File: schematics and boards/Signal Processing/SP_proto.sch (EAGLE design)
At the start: 30 parts, among them IC1 MAX490CPA+, IC2 MAX490CPA+, IC3 MAX490CPA+, IC4 MAX490CPA+, IC6 MEGA164-P, IC7 MAX490CPA+, Q1 20MHz

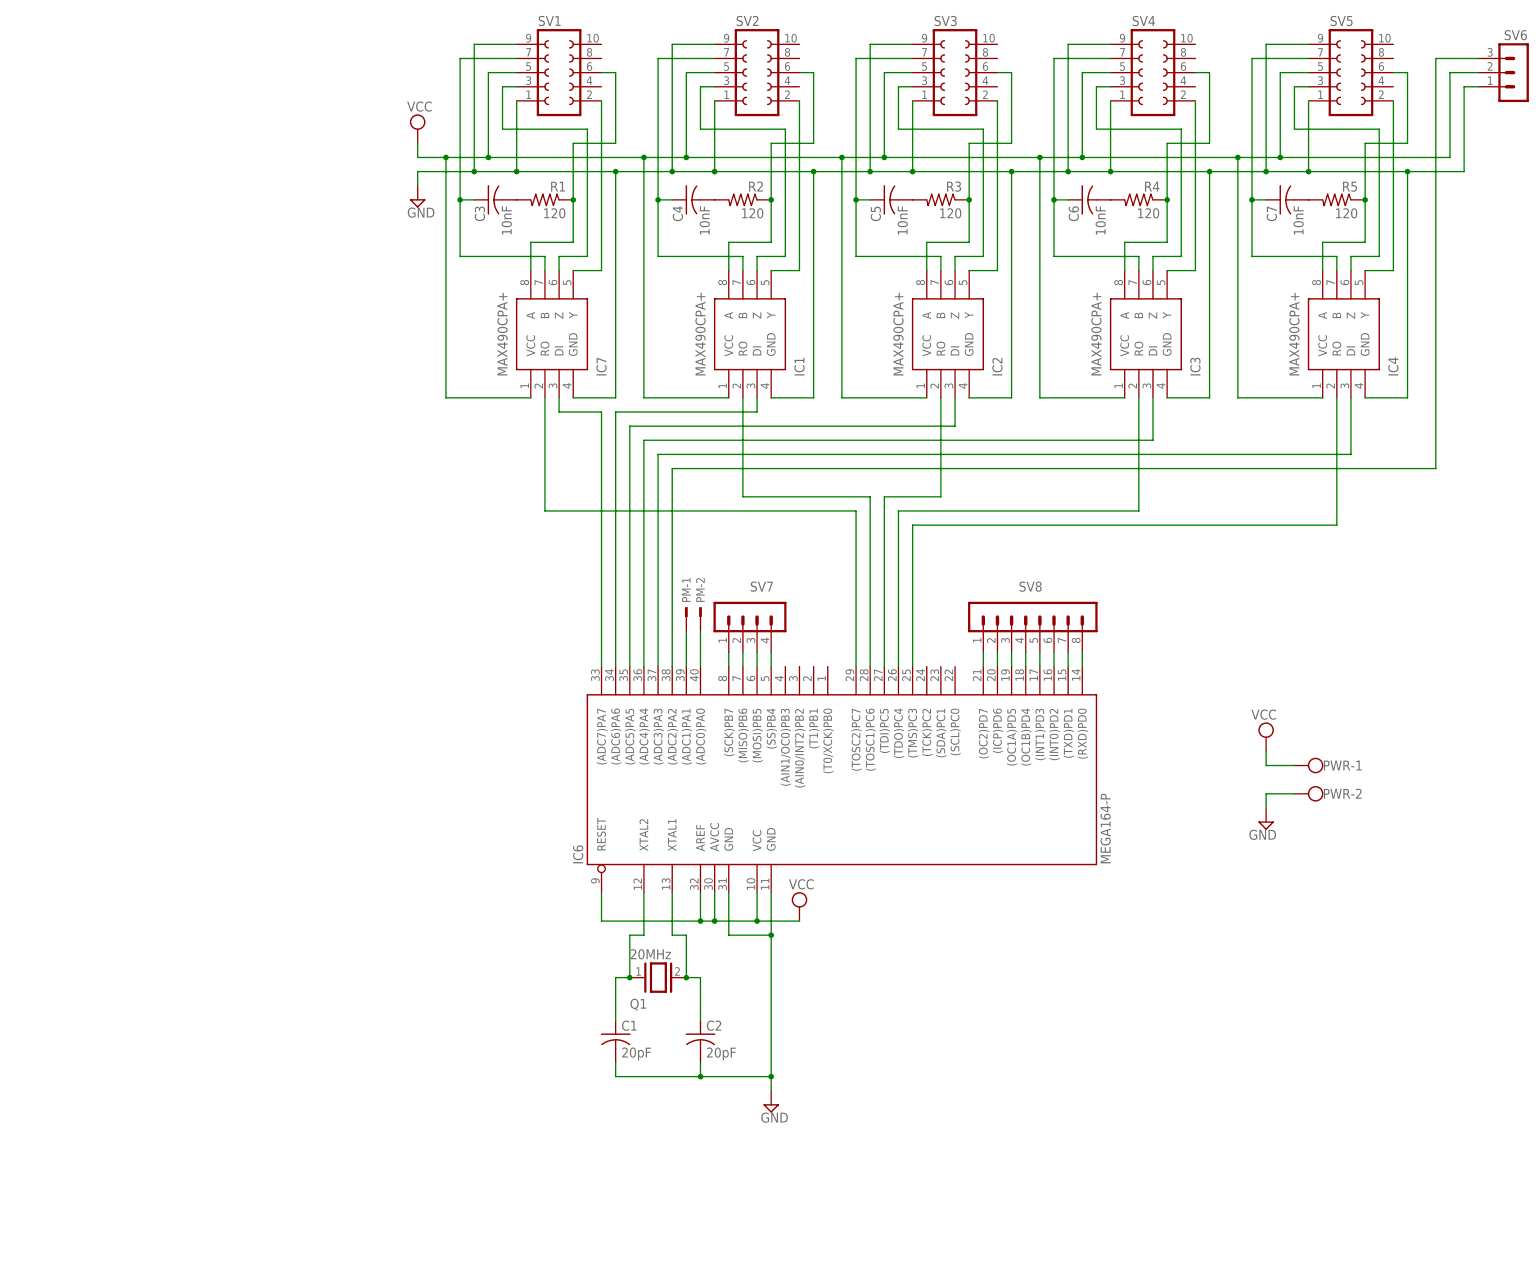
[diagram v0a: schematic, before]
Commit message: Made a small change in the Power Distribution board within the new 5th version. Cleaned up the schematic names and got rid of outdated or useless schematic and board files.
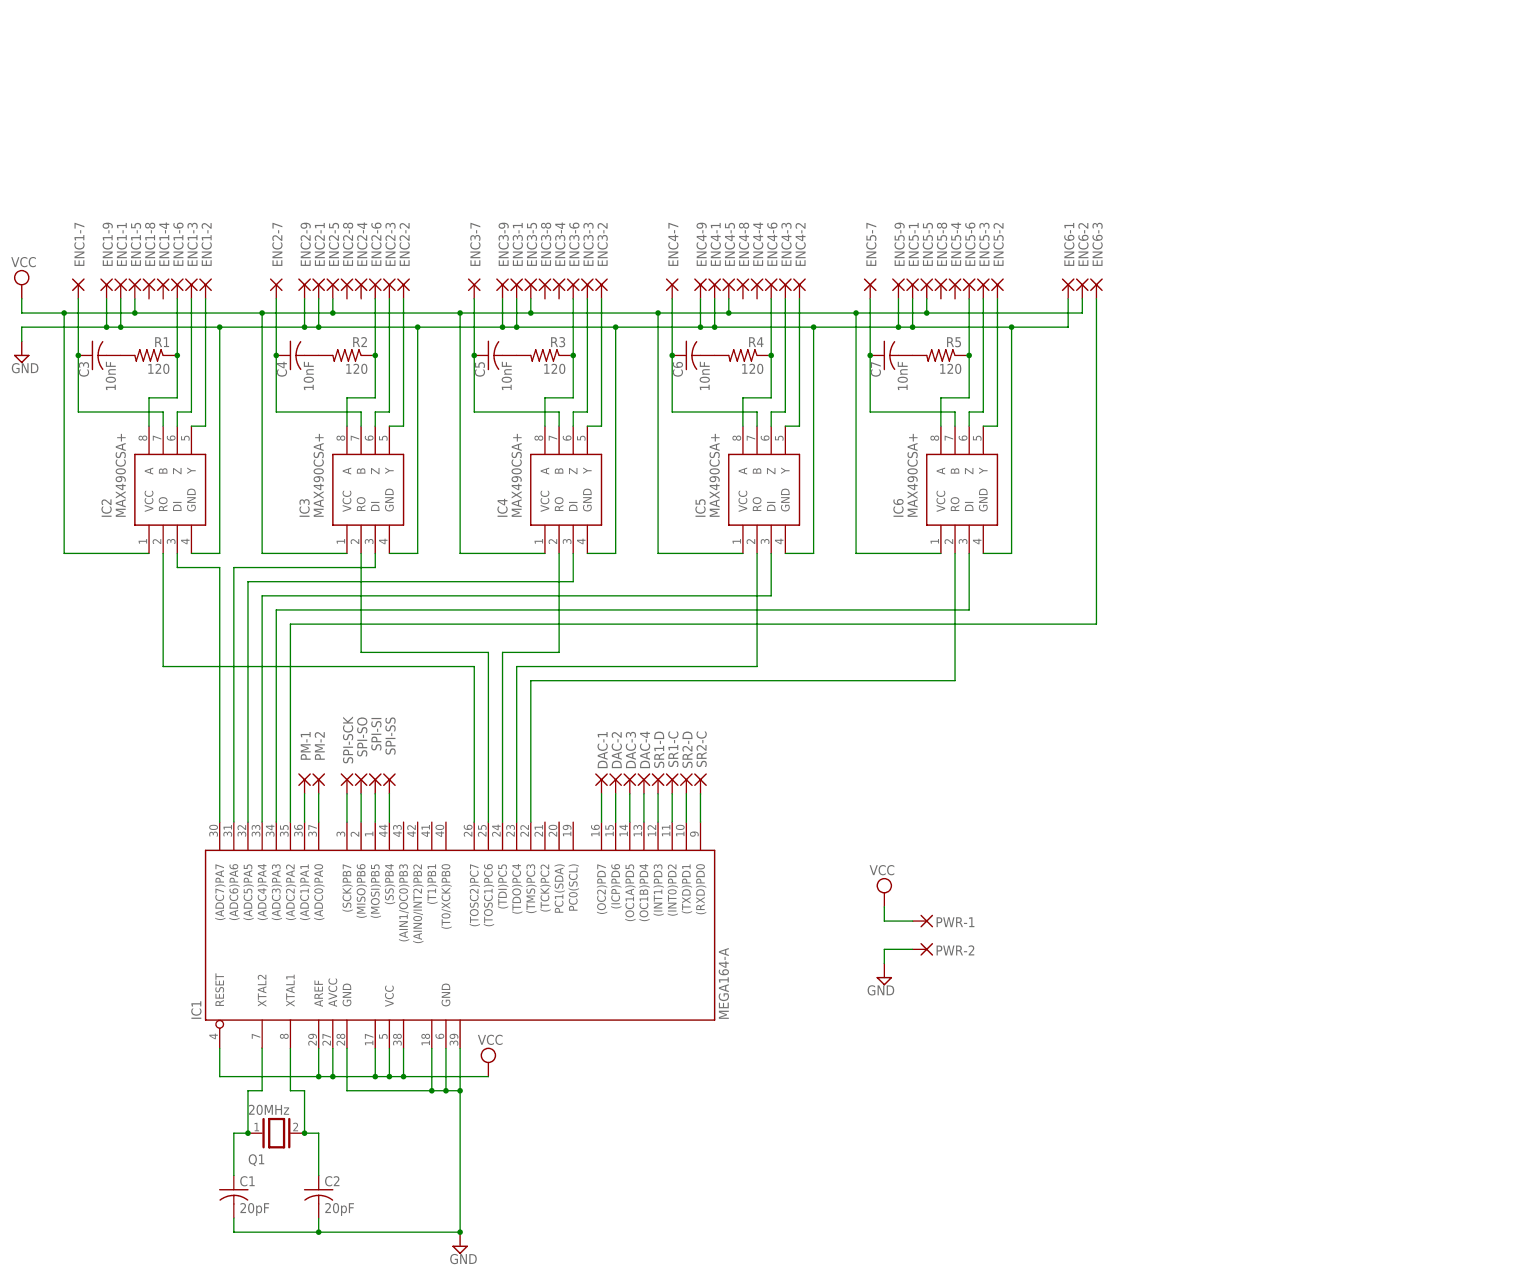
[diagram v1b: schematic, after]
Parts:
- removed IC7: MAX490CPA+, rasm_parts:MAX490CPA+
- removed PWR: (no value), con-wago-500:W237-102
- removed SV1, SV2, SV3, SV4, SV5: (no value), con-lsta:FE05-2
- removed SV6: (no value), con-lstb:MA03-1
- removed SV7: (no value), con-lstb:MA04-1
- removed SV8: (no value), con-lstb:MA08-1W
- added DAC-1, DAC-2, DAC-3, DAC-4, ENC1-1, ENC1-2, ENC1-3, ENC1-4, ENC1-5, ENC1-6, ENC1-7, ENC1-8, ENC1-9, ENC2-1, ENC2-2, ENC2-3, ENC2-4, ENC2-5, ENC2-6, ENC2-7, ENC2-8, ENC2-9, ENC3-1, ENC3-2, ENC3-3, ENC3-4, ENC3-5, ENC3-6, ENC3-7, ENC3-8, ENC3-9, ENC4-1, ENC4-2, ENC4-3, ENC4-4, ENC4-5, ENC4-6, ENC4-7, ENC4-8, ENC4-9, ENC5-1, ENC5-2, ENC5-3, ENC5-4, ENC5-5, ENC5-6, ENC5-7, ENC5-8, ENC5-9, ENC6-1, ENC6-2, ENC6-3, PWR-1, PWR-2, SPI-SCK, SPI-SI, SPI-SO, SPI-SS, SR1-C, SR1-D, SR2-C, SR2-D: (no value), wirepad:1,6/0,8
- added IC5: MAX490CSA+, rasm_parts:MAX490CSA+
- IC1: value MAX490CPA+ -> MEGA164-A; device rasm_parts:MAX490CPA+ -> atmel:MEGA16-A
- IC2, IC3, IC4: value MAX490CPA+ -> MAX490CSA+; device rasm_parts:MAX490CPA+ -> rasm_parts:MAX490CSA+
- IC6: value MEGA164-P -> MAX490CSA+; device atmel:MEGA16-P -> rasm_parts:MAX490CSA+
- PM-1, PM-2: value TSW-101-07-G-S -> (none); device con-samtec:TSW-101-07-G-S -> wirepad:1,6/0,8
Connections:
- removed net N$12 (its old number): IC1.A, R2.1, SV2.6
- removed net N$17 (its old number): IC2.A, R3.1, SV3.6
- removed net N$22 (its old number): IC3.A, R4.1, SV4.6
- removed net N$25: IC4.Y, SV5.2
- removed net N$26: IC4.Z, SV5.3
- removed net N$27: IC6.(ADC2)PA2, SV6.3
- removed net N$28: IC6.(ADC7)PA7, IC7.DI
- removed net N$29: IC1.DI, IC6.(ADC6)PA6
- removed net N$30: IC2.DI, IC6.(ADC5)PA5
- removed net N$31: IC3.DI, IC6.(ADC4)PA4
- removed net N$32: IC4.DI, IC6.(ADC3)PA3
- removed net N$33: IC6.(TOSC2)PC7, IC7.RO
- removed net N$34: IC1.RO, IC6.(TOSC1)PC6
- removed net N$35: IC2.RO, IC6.(TDI)PC5
- removed net N$37: IC4.RO, IC6.(TMS)PC3
- removed net N$38: IC3.RO, IC6.(TDO)PC4
- removed net N$41: IC6.(OC1B)PD4, SV8.4
- removed net N$42: SV2.7
- removed net N$43: IC4.A, R5.1, SV5.6
- removed net N$44: SV5.7
- removed net N$46: IC6.(ADC1)PA1, PM-1.1
- removed net N$47: IC6.(INT1)PD3, SV8.5
- removed net N$48: IC6.(INT0)PD2, SV8.6
- removed net N$49: IC6.(TXD)PD1, SV8.7
- removed net N$50: IC6.(RXD)PD0, SV8.8
- removed net N$52: SV3.7
- removed net N$7 (its old number): IC7.Y, SV1.2
- new net N$104: C3.1, ENC1-7.P, IC2.B
- new net N$14: ENC4-2.P, IC5.Y
- new net N$19: ENC5-2.P, IC6.Y
- new net N$61: IC1.(TDI)PC5, IC4.RO
- new net N$62: IC1.(TMS)PC3, IC6.RO
- new net N$64: IC1.(TDO)PC4, IC5.RO
- new net N$67: DAC-1.P, IC1.(OC2)PD7
- new net N$68: DAC-2.P, IC1.(ICP)PD6
- new net N$69: DAC-3.P, IC1.(OC1A)PD5
- new net N$70: DAC-4.P, IC1.(OC1B)PD4
- new net N$71: IC1.(INT1)PD3, SR1-D.P
- new net N$72: IC1.(INT0)PD2, SR1-C.P
- new net N$73: IC1.(TXD)PD1, SR2-D.P
- new net N$74: IC1.(RXD)PD0, SR2-C.P
- new net N$75: IC1.(ADC1)PA1, PM-1.P
- new net N$76: IC1.(ADC0)PA0, PM-2.P
- new net N$79: IC1.(ADC7)PA7, IC2.DI
- new net N$80: ENC1-6.P, IC2.A, R1.1
- new net N$9: ENC3-2.P, IC4.Y
- net GND: now also ENC1-1.P, ENC1-9.P, ENC2-1.P, ENC2-9.P, ENC3-1.P, ENC3-9.P, ENC4-1.P, ENC4-9.P, ENC5-1.P, ENC5-9.P, ENC6-1.P, IC1.GND1, IC1.GND2, IC1.GND@1, IC5.GND, PWR-2.P; no longer IC6.GND@1, IC7.GND, PWR-2.KL, SV1.1, SV1.9, SV2.1, SV2.9, SV3.1, SV3.9, SV4.1, SV4.9, SV5.1, SV5.9, SV6.1
- net N$1: now also IC1.(SS)PB4, SPI-SS.P; no longer IC6.(SCK)PB7, SV7.1
- net N$10: now also ENC3-3.P, IC4.Z; no longer IC1.Y, SV2.2
- net N$11: now also ENC3-6.P, IC4.A, R3.1; no longer IC1.Z, SV2.3
- net N$13: now also C5.1, ENC3-7.P, IC4.B; no longer IC1.B
- net N$15: now also ENC4-3.P, IC5.Z; no longer IC2.Y, SV3.2
- net N$16: now also ENC4-6.P, IC5.A, R4.1; no longer IC2.Z, SV3.3
- net N$18: now also C6.1, ENC4-7.P, IC5.B; no longer IC2.B
- net N$2: now also IC1.(MOSI)PB5, SPI-SI.P; no longer IC6.(MISO)PB6, SV7.2
- net N$20: now also ENC5-3.P, IC6.Z; no longer IC3.Y, SV4.2
- net N$21: now also ENC5-6.P, IC6.A, R5.1; no longer IC3.Z, SV4.3
- net N$23: now also C7.1, ENC5-7.P, IC6.B; no longer SV4.7
- net N$3: now also ENC2-2.P, IC3.Y; no longer IC6.(OC2)PD7, SV8.1
- net N$36: now also IC1.XTAL2; no longer IC6.XTAL2
- net N$39: now also IC1.XTAL1; no longer IC6.XTAL1
- net N$4: now also ENC2-3.P, IC3.Z; no longer IC6.(ICP)PD6, SV8.2
- net N$40: now also IC1.(SCK)PB7, SPI-SCK.P; no longer IC6.(SS)PB4, SV7.4
- net N$5: now also ENC2-6.P, IC3.A, R2.1; no longer IC6.(OC1A)PD5, SV8.3
- net N$51: now also ENC1-2.P, IC2.Y; no longer C3.1, IC7.B, SV1.7
- net N$53: now also ENC1-3.P, IC2.Z; no longer IC3.B
- net N$54: now also ENC6-3.P, IC1.(ADC2)PA2; no longer IC6.(ADC0)PA0, PM-2.1
- net N$55: now also IC1.(ADC6)PA6, IC3.DI; no longer IC7.A, R1.1, SV1.6
- net N$56: now also IC1.(ADC5)PA5, IC4.DI; no longer IC4.B
- net N$57: now also IC1.(ADC4)PA4, IC5.DI; no longer C4.1
- net N$58: now also IC1.(ADC3)PA3, IC6.DI; no longer C5.1
- net N$59: now also IC1.(TOSC2)PC7, IC2.RO; no longer C6.1
- net N$6: now also IC1.(MISO)PB6, SPI-SO.P; no longer IC6.(MOSI)PB5, SV7.3
- net N$60: now also IC1.(TOSC1)PC6, IC3.RO; no longer C7.1
- net N$8: now also C4.1, ENC2-7.P, IC3.B; no longer IC7.Z, SV1.3
- net VCC: now also ENC1-5.P, ENC2-5.P, ENC3-5.P, ENC4-5.P, ENC5-5.P, ENC6-2.P, IC1.AREF, IC1.AVCC, IC1.RESET, IC1.VCC1, IC1.VCC2, IC5.VCC, PWR-1.P; no longer IC6.AREF, IC6.AVCC, IC6.RESET, IC7.VCC, PWR-1.KL, SV1.5, SV2.5, SV3.5, SV4.5, SV5.5, SV6.2
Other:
- moved on the sheet: C1, C2, C3, C4, C5, C6, C7, IC2, IC3, IC4, Q1, R1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
